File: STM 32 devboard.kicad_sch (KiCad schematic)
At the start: 29 parts, among them J1 Conn_01x10_Pin, J2 Conn_01x10_Pin, J3 USB_B_Micro, SW1 SW_SPDT, U1 AMS1117-3.3, U2 STM32F103C8T6, Y1 16MHz

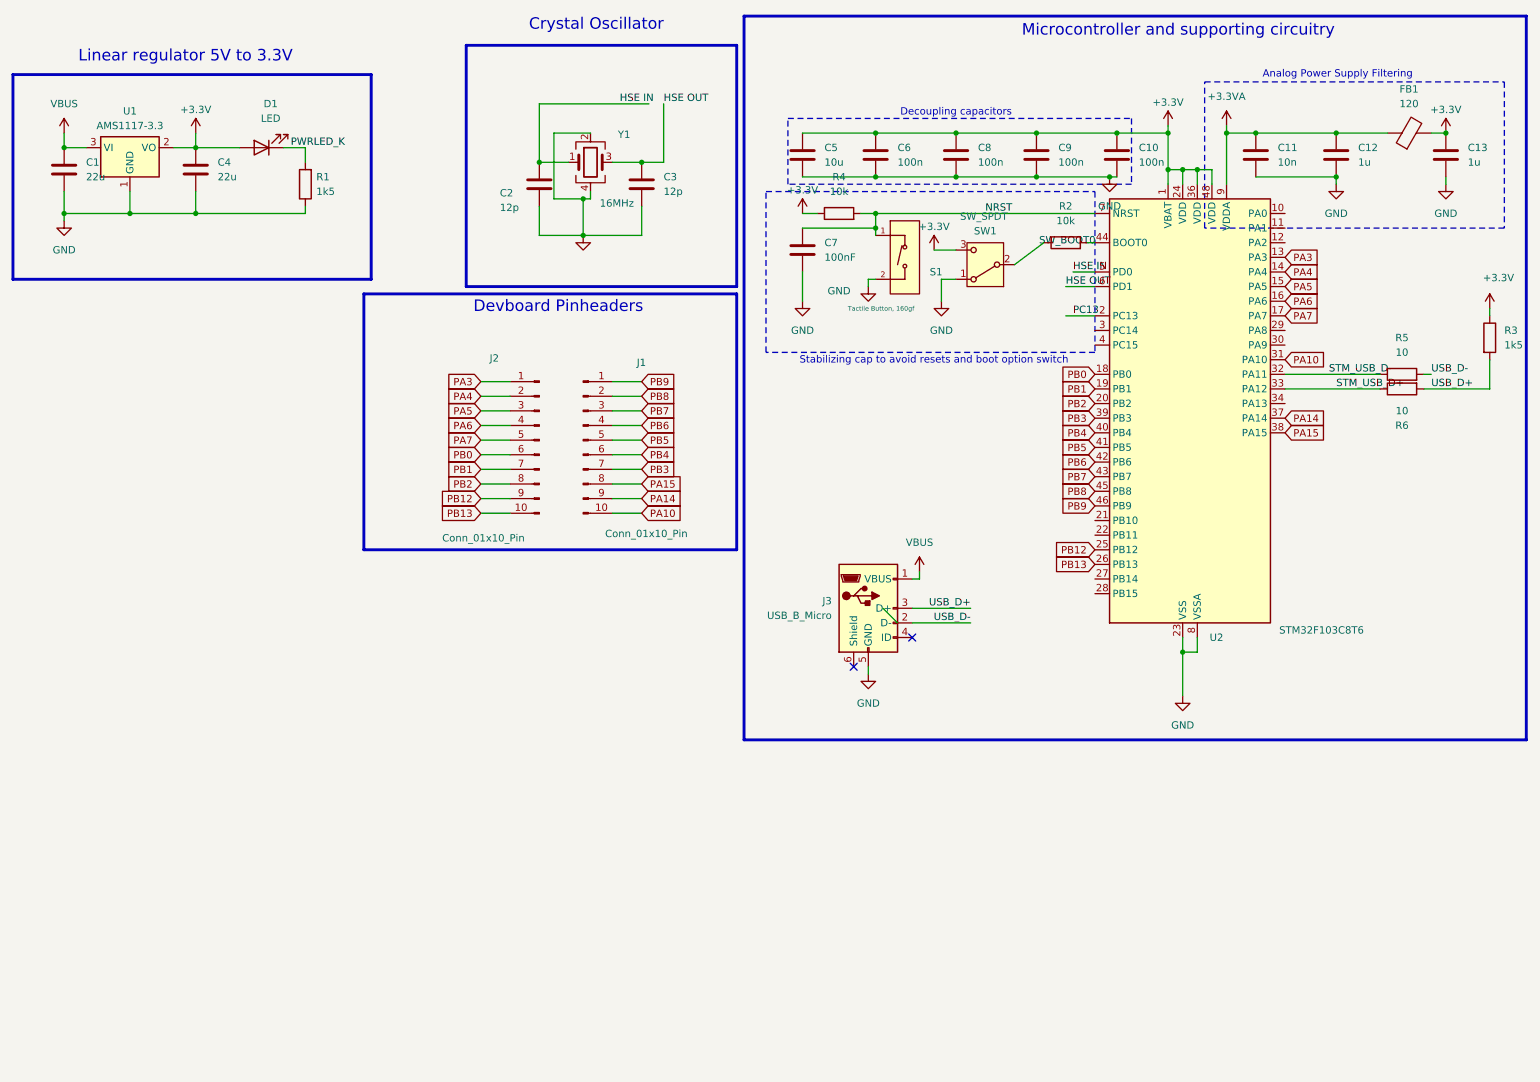
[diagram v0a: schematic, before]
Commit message: Added USB-C port.
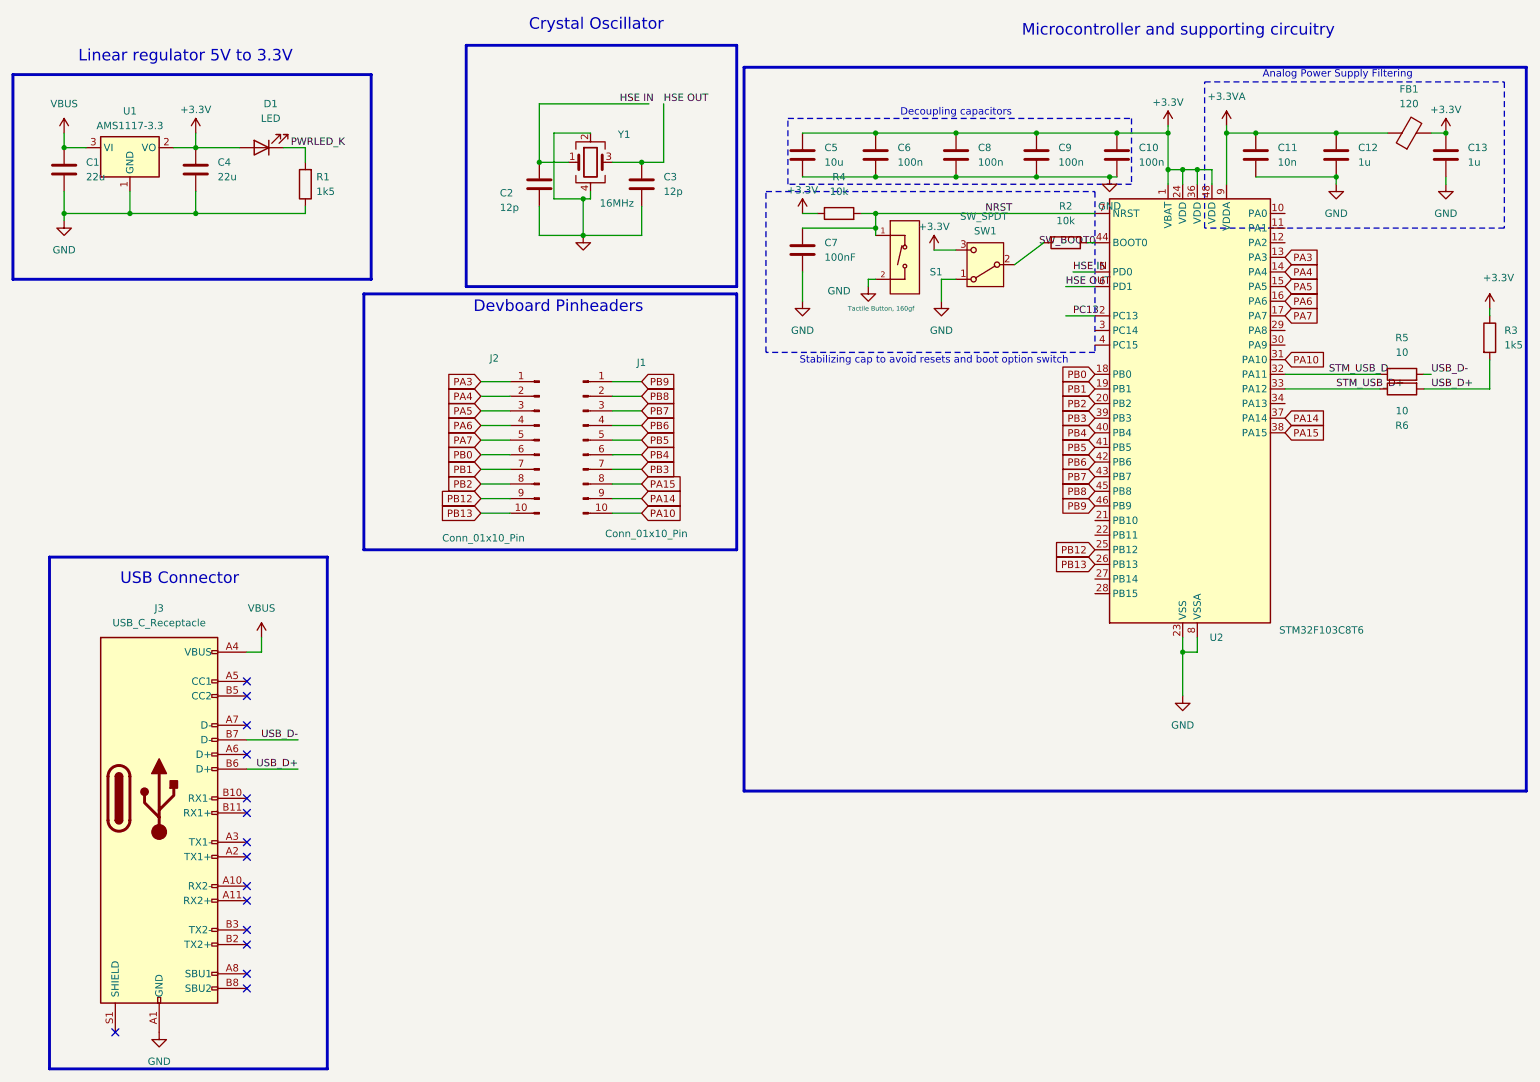
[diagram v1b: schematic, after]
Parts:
- removed J3: USB_B_Micro, Connector_USB:USB_Micro-B_Molex-105017-0001, symbol Connector:USB_B_Micro
- added J3: USB_C_Receptacle, Connector_USB:USB_C_Receptacle_GCT_USB4110, symbol Connector:USB_C_Receptacle
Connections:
- net GND: now also J3.A1 (GND), J3.A12 (GND), J3.B1 (GND), J3.B12 (GND)
- net USB_D+: now also J3.B6 (D+)
- net USB_D-: now also J3.B7 (D-)
- net VBUS: now also J3.A4 (VBUS), J3.A9 (VBUS), J3.B4 (VBUS), J3.B9 (VBUS)
- no-connect marks 2 -> 15
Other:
- note added: "USB Connector"
